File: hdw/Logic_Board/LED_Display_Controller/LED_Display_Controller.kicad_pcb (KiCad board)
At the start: 4 copper layers, 855 parts, among them J1101 USB_B_Mini, J1401 Encoder Ext, J1601 POS5P EXT, J1602 POS5P PGOOD, J1603 POS5P_THWN, J1604 POS5P_RUN, J201 +12V IN, J202 GND IN, J203 +12V IN AUX, J204 Master Power SW, J2901 STRING 1, J2902 STRING 2, J2903 STRING 3, J2904 STRING 4, J3001 USB UART, J3002 WIFI UART, J3003 FLASH SPI, J3004 Panel TP, J501 PICKIT3, J901 ESP8266 Socket, Q201 IPC100N04S51R7ATMA1, Q202 IPC100N04S51R7ATMA1, Q501 BSS214NW, Q901 BSS214NW, SW1401 Display Enable, SW1402 Brightness/Enable, SW501 MRST, U1001 ISO7321C, U1101 LT6700-1-S6, U1102 FT234XD, U1103 74LVC1G06, U1104 TPD3S014DBVR, U1201 74LVC1G06, U1202 74LVC1G06, U1203 74LVC1G06, U1204 74LVC1G06, U1205 74LVC1G06, U1206 74LVC1G06, U1207 74LVC1G06, U1301 74LVC1G06, U1302 74LVC1G06, U1303 74LVC1G06, U1304 74LVC1G06, U1401 MAX6816, U1402 74LVC2G14, U1403 74LVC1G79, U1601 LM1117-ADJ, U1602 NUP2202, U1603 74LVC1G17, U1604 74LVC1G17, U1605 74LVC1G17, U1606 NUP2202, U1701 CY7C1010DV33, U1801 SST25PF020B, U1901 SST25PF020B, U2001 SST25PF020B, U201 LTC4365DDB, U2101 SST25PF020B, U2201 SST25PF020B, U2301 SST25PF020B, U2401 SST25PF020B, U2501 SST25PF020B, U2601 74HCT541, U2602 74HCT541, U2701 74HCT541, U2702 74HCT541, U2801 74LVC1G32, U2802 74HCT541, U301 LTC3605A_UF, U401 LTC3624DD, U601 PIC32MZ2048EFH144_IPL

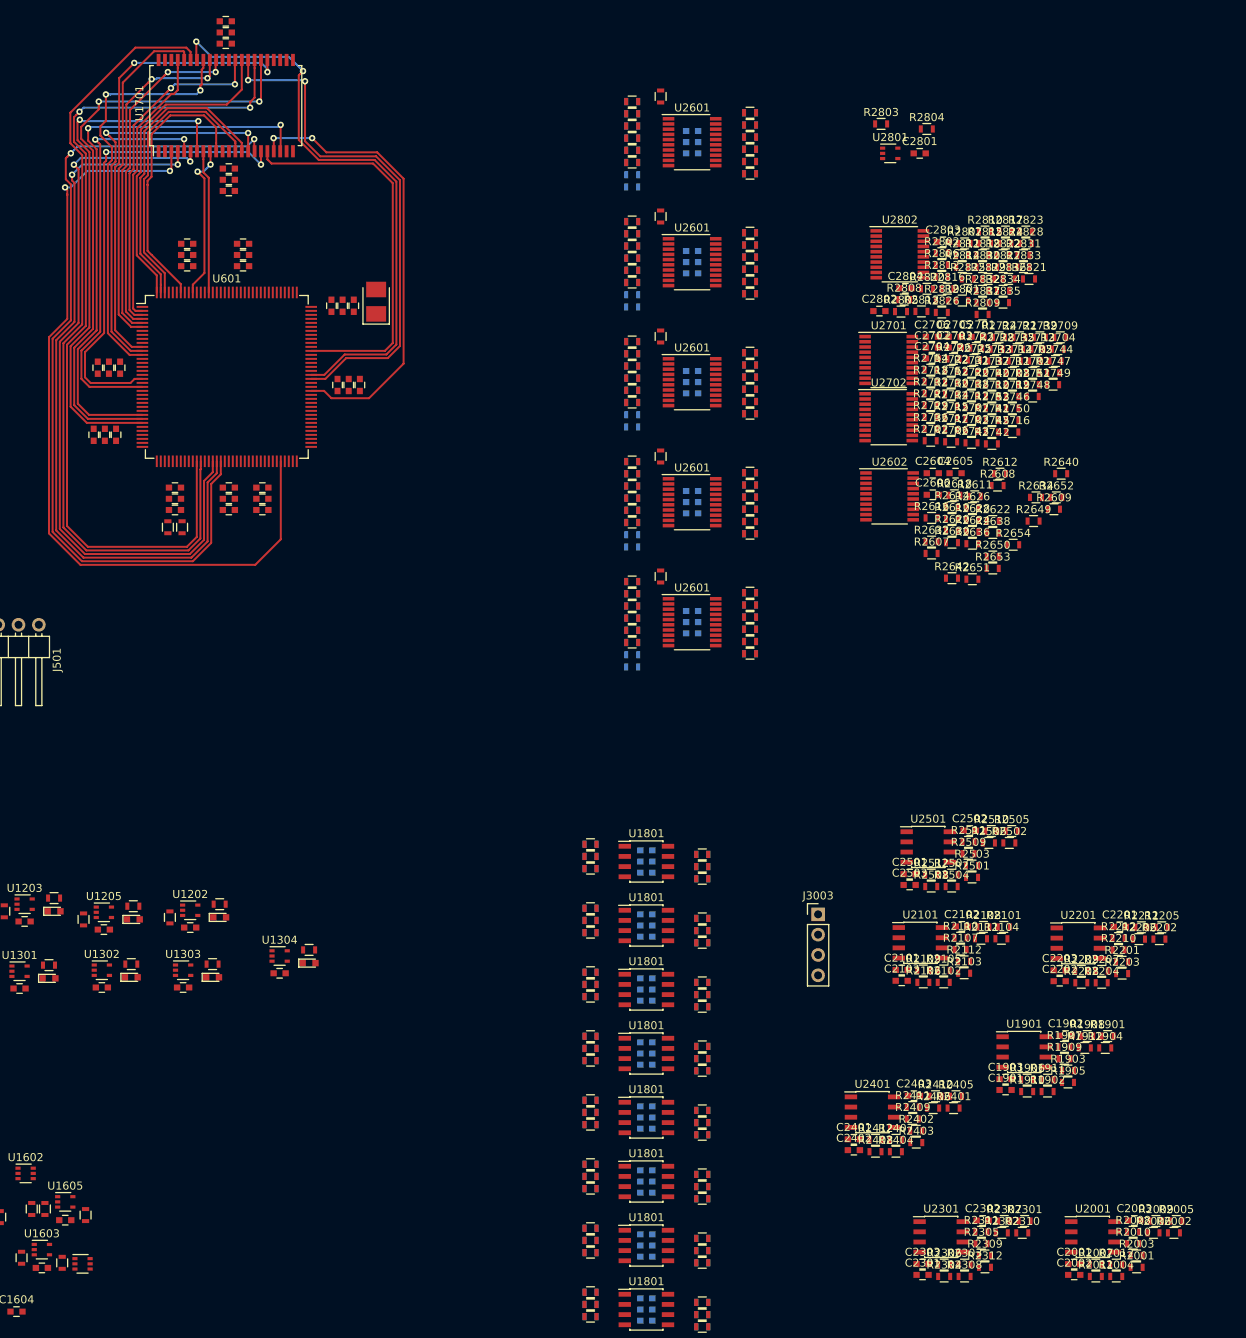
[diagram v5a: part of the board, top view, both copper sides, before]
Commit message: Fixed FLASH reference designators
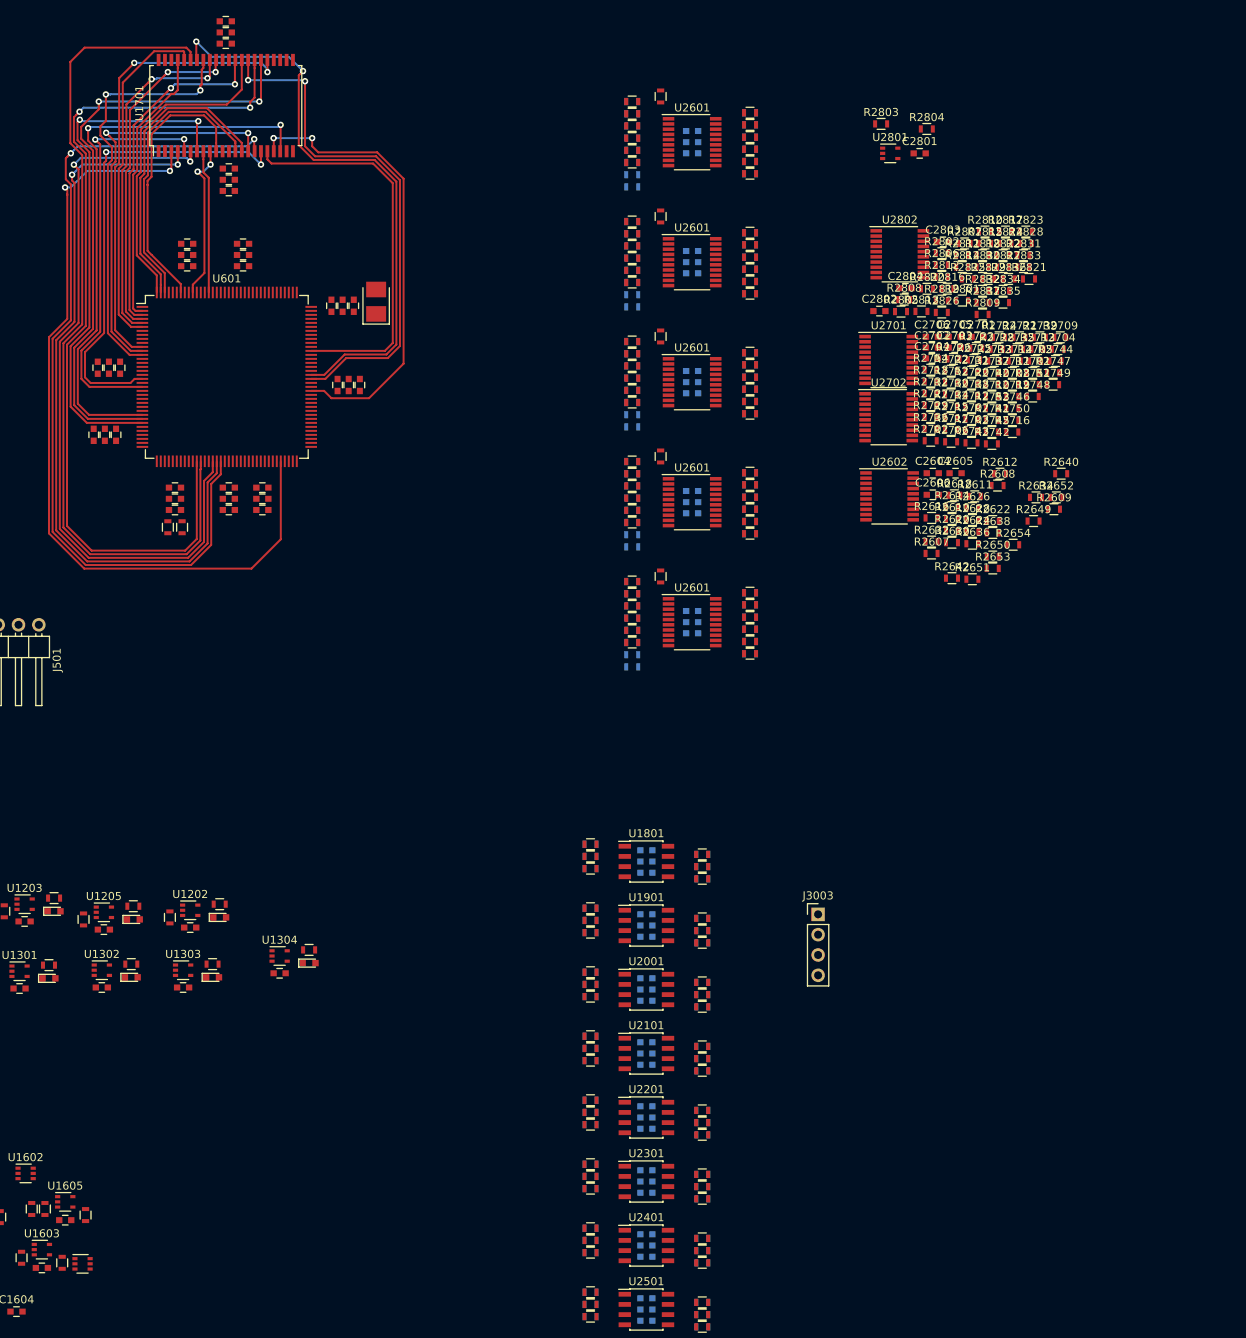
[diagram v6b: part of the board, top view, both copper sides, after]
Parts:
- removed the C1901 at (168.2, 156.6)
- removed the C1902 at (175.7, 149.8)
- removed the C1903 at (168.2, 155.2)
- removed the C2001 at (176.8, 178.3)
- removed the C2002 at (176.8, 179.7)
- removed the C2003 at (184.3, 172.9)
- removed the C2101 at (155.2, 141.6)
- removed the C2102 at (162.7, 136.1)
- removed the C2103 at (155.2, 142.9)
- removed the C2201 at (182.5, 136.2)
- removed the C2202 at (175.0, 143.0)
- removed the C2203 at (175.0, 141.6)
- removed the C2301 at (157.8, 179.7)
- removed the C2302 at (165.3, 172.9)
- removed the C2303 at (157.8, 178.3)
- removed the C2401 at (149.3, 162.7)
- removed the C2402 at (149.3, 164.1)
- removed the C2403 at (156.8, 157.3)
- removed the C2501 at (156.2, 129.6)
- removed the C2502 at (163.7, 124.1)
- removed the C2503 at (156.2, 130.9)
- removed the R1901 at (181.0, 149.8)
- removed the R1902 at (173.5, 156.8)
- removed the R1903 at (176.0, 154.1)
- removed the R1904 at (180.7, 151.3)
- removed the R1905 at (176.0, 155.6)
- removed the R1906 at (170.9, 155.3)
- removed the R1907 at (175.6, 151.2)
- removed the R1908 at (178.4, 149.8)
- removed the R1909 at (175.6, 152.7)
- removed the R1910 at (170.9, 156.8)
- removed the R1911 at (173.5, 155.3)
- removed the R1912 at (178.1, 151.3)
- removed the R2001 at (184.6, 178.7)
- removed the R2002 at (189.3, 174.4)
- removed the R2003 at (184.6, 177.3)
- removed the R2004 at (182.0, 179.9)
- removed the R2005 at (189.6, 173.0)
- removed the R2006 at (186.7, 174.4)
- removed the R2007 at (179.5, 178.4)
- removed the R2008 at (184.2, 174.3)
- removed the R2009 at (187.0, 173.0)
- removed the R2010 at (184.2, 175.8)
- removed the R2011 at (179.5, 179.9)
- removed the R2012 at (182.0, 178.4)
- removed the R2101 at (168.0, 136.2)
- removed the R2102 at (160.5, 143.1)
- removed the R2103 at (163.0, 142.0)
- removed the R2104 at (167.7, 137.7)
- removed the R2105 at (160.5, 141.6)
- removed the R2106 at (157.9, 143.1)
- removed the R2107 at (162.6, 139.0)
- removed the R2108 at (165.4, 136.2)
- removed the R2109 at (157.9, 141.6)
- removed the R2110 at (162.6, 137.5)
- removed the R2111 at (165.1, 137.7)
- removed the R2112 at (163.0, 140.5)
- removed the R2201 at (182.8, 140.5)
- removed the R2202 at (187.4, 137.7)
- removed the R2203 at (182.8, 142.0)
- removed the R2204 at (180.2, 143.2)
- removed the R2205 at (187.7, 136.2)
- removed the R2206 at (184.9, 137.7)
- removed the R2207 at (180.2, 141.7)
- removed the R2208 at (177.7, 143.2)
- removed the R2209 at (177.7, 141.7)
- removed the R2210 at (182.3, 139.1)
- removed the R2211 at (185.2, 136.2)
- removed the R2212 at (182.3, 137.6)
- removed the R2301 at (170.6, 173.0)
- removed the R2302 at (167.7, 174.4)
- removed the R2303 at (163.1, 178.4)
- removed the R2304 at (160.5, 179.9)
- removed the R2305 at (165.2, 175.8)
- removed the R2306 at (160.5, 178.4)
- removed the R2307 at (168.0, 173.0)
- removed the R2308 at (163.1, 179.9)
- removed the R2309 at (165.6, 177.3)
- removed the R2310 at (170.3, 174.4)
- removed the R2311 at (165.2, 174.3)
- removed the R2312 at (165.6, 178.7)
- removed the R2401 at (161.7, 158.8)
- removed the R2402 at (157.1, 161.7)
- removed the R2403 at (157.1, 163.1)
- removed the R2404 at (154.5, 164.3)
- removed the R2405 at (162.0, 157.4)
- removed the R2406 at (159.2, 158.8)
- removed the R2407 at (154.5, 162.8)
- removed the R2408 at (152.0, 164.3)
- removed the R2409 at (156.6, 160.2)
- removed the R2410 at (159.5, 157.4)
- removed the R2411 at (156.6, 158.7)
- removed the R2412 at (152.0, 162.8)
- removed the R2501 at (164.0, 130.0)
- removed the R2502 at (168.7, 125.7)
- removed the R2503 at (164.0, 128.5)
- removed the R2504 at (161.5, 131.1)
- removed the R2505 at (169.0, 124.2)
- removed the R2506 at (166.1, 125.7)
- removed the R2507 at (161.5, 129.7)
- removed the R2508 at (158.9, 131.1)
- removed the R2509 at (163.6, 127.0)
- removed the R2510 at (166.4, 124.2)
- removed the R2511 at (163.6, 125.6)
- removed the R2512 at (158.9, 129.7)
- removed the U1901 at (170.5, 151.8)
- removed the U2001 at (179.1, 174.9)
- removed the U2101 at (157.6, 138.2)
- removed the U2201 at (177.3, 138.2)
- removed the U2301 at (160.2, 174.9)
- removed the U2401 at (151.6, 159.3)
- removed the U2501 at (158.6, 126.2)
- renumbered C1801 to C1901, C1802 to C1902, C1803 to C1903, C1801 to C2001, C1802 to C2002, C1803 to C2003, C1801 to C2101, C1802 to C2102, C1803 to C2103, C1801 to C2201, C1802 to C2202, C1803 to C2203, C1801 to C2301, C1802 to C2302, C1803 to C2303, C1801 to C2401, C1802 to C2402, C1803 to C2403, C1801 to C2501, C1802 to C2502, C1803 to C2503, R1801 to R1901, R1802 to R1902, R1803 to R1903, R1804 to R1904, R1805 to R1905, R1806 to R1906, R1807 to R1907, R1808 to R1908, R1809 to R1909, R1810 to R1910, R1811 to R1911, R1812 to R1912, R1801 to R2001, R1802 to R2002, R1803 to R2003, R1804 to R2004, R1805 to R2005, R1806 to R2006, R1807 to R2007, R1808 to R2008, R1809 to R2009, R1810 to R2010, R1811 to R2011, R1812 to R2012, R1801 to R2101, R1802 to R2102, R1803 to R2103, R1804 to R2104, R1805 to R2105, R1806 to R2106, R1807 to R2107, R1808 to R2108, R1809 to R2109, R1810 to R2110, R1811 to R2111, R1812 to R2112, R1801 to R2201, R1802 to R2202, R1803 to R2203, R1804 to R2204, R1805 to R2205, R1806 to R2206, R1807 to R2207, R1808 to R2208, R1809 to R2209, R1810 to R2210, R1811 to R2211, R1812 to R2212, R1801 to R2301, R1802 to R2302, R1803 to R2303, R1804 to R2304, R1805 to R2305, R1806 to R2306, R1807 to R2307, R1808 to R2308, R1809 to R2309, R1810 to R2310, R1811 to R2311, R1812 to R2312, R1801 to R2401, R1802 to R2402, R1803 to R2403, R1804 to R2404, R1805 to R2405, R1806 to R2406, R1807 to R2407, R1808 to R2408, R1809 to R2409, R1810 to R2410, R1811 to R2411, R1812 to R2412, R1801 to R2501, R1802 to R2502, R1803 to R2503, R1804 to R2504, R1805 to R2505, R1806 to R2506, R1807 to R2507, R1808 to R2508, R1809 to R2509, R1810 to R2510, R1811 to R2511, R1812 to R2512, U1801 to U1901, U1801 to U2001, U1801 to U2101, U1801 to U2201, U1801 to U2301, U1801 to U2401, U1801 to U2501
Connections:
- R1901 pad 1: Net-(R1801-Pad1) -> Net-(R1901-Pad1)
- R1902 pad 1: Net-(R1802-Pad1) -> Net-(R1902-Pad1)
- R1903 pad 1: Net-(R1803-Pad1) -> Net-(R1903-Pad1)
- R1903 pad 2: ~FLASH_WP1 -> ~FLASH_WP2
- R1904 pad 1: Net-(R1804-Pad1) -> Net-(R1904-Pad1)
- R1904 pad 2: ~FLASH_CE1 -> ~FLASH_CE2
- R1905 pad 1: Net-(R1805-Pad1) -> Net-(R1905-Pad1)
- R1906 pad 2: Net-(R1803-Pad1) -> Net-(R1903-Pad1)
- R1907 pad 2: Net-(R1804-Pad1) -> Net-(R1904-Pad1)
- R1908 pad 1: Net-(R1805-Pad1) -> Net-(R1905-Pad1)
- R1909 pad 2: Net-(R1802-Pad1) -> Net-(R1902-Pad1)
- R1910 pad 1: Net-(R1801-Pad1) -> Net-(R1901-Pad1)
- R1911 pad 1: Net-(R1811-Pad1) -> Net-(R1911-Pad1)
- R1912 pad 2: Net-(R1811-Pad1) -> Net-(R1911-Pad1)
- R2001 pad 1: Net-(R1801-Pad1) -> Net-(R2001-Pad1)
- R2002 pad 1: Net-(R1802-Pad1) -> Net-(R2002-Pad1)
- R2003 pad 1: Net-(R1803-Pad1) -> Net-(R2003-Pad1)
- R2003 pad 2: ~FLASH_WP1 -> ~FLASH_WP3
- R2004 pad 1: Net-(R1804-Pad1) -> Net-(R2004-Pad1)
- R2004 pad 2: ~FLASH_CE1 -> ~FLASH_CE3
- R2005 pad 1: Net-(R1805-Pad1) -> Net-(R2005-Pad1)
- R2006 pad 2: Net-(R1803-Pad1) -> Net-(R2003-Pad1)
- R2007 pad 2: Net-(R1804-Pad1) -> Net-(R2004-Pad1)
- R2008 pad 1: Net-(R1805-Pad1) -> Net-(R2005-Pad1)
- R2009 pad 2: Net-(R1802-Pad1) -> Net-(R2002-Pad1)
- R2010 pad 1: Net-(R1801-Pad1) -> Net-(R2001-Pad1)
- R2011 pad 1: Net-(R1811-Pad1) -> Net-(R2011-Pad1)
- R2012 pad 2: Net-(R1811-Pad1) -> Net-(R2011-Pad1)
- R2101 pad 1: Net-(R1801-Pad1) -> Net-(R2101-Pad1)
- R2102 pad 1: Net-(R1802-Pad1) -> Net-(R2102-Pad1)
- R2103 pad 1: Net-(R1803-Pad1) -> Net-(R2103-Pad1)
- R2103 pad 2: ~FLASH_WP1 -> ~FLASH_WP4
- R2104 pad 1: Net-(R1804-Pad1) -> Net-(R2104-Pad1)
- R2104 pad 2: ~FLASH_CE1 -> ~FLASH_CE4
- R2105 pad 1: Net-(R1805-Pad1) -> Net-(R2105-Pad1)
- R2106 pad 2: Net-(R1803-Pad1) -> Net-(R2103-Pad1)
- R2107 pad 2: Net-(R1804-Pad1) -> Net-(R2104-Pad1)
- R2108 pad 1: Net-(R1805-Pad1) -> Net-(R2105-Pad1)
- R2109 pad 2: Net-(R1802-Pad1) -> Net-(R2102-Pad1)
- R2110 pad 1: Net-(R1801-Pad1) -> Net-(R2101-Pad1)
- R2111 pad 1: Net-(R1811-Pad1) -> Net-(R2111-Pad1)
- R2112 pad 2: Net-(R1811-Pad1) -> Net-(R2111-Pad1)
- R2201 pad 1: Net-(R1801-Pad1) -> Net-(R2201-Pad1)
- R2202 pad 1: Net-(R1802-Pad1) -> Net-(R2202-Pad1)
- R2203 pad 1: Net-(R1803-Pad1) -> Net-(R2203-Pad1)
- R2203 pad 2: ~FLASH_WP1 -> ~FLASH_WP5
- R2204 pad 1: Net-(R1804-Pad1) -> Net-(R2204-Pad1)
- R2204 pad 2: ~FLASH_CE1 -> ~FLASH_CE5
- R2205 pad 1: Net-(R1805-Pad1) -> Net-(R2205-Pad1)
- R2206 pad 2: Net-(R1803-Pad1) -> Net-(R2203-Pad1)
- R2207 pad 2: Net-(R1804-Pad1) -> Net-(R2204-Pad1)
- R2208 pad 1: Net-(R1805-Pad1) -> Net-(R2205-Pad1)
- R2209 pad 2: Net-(R1802-Pad1) -> Net-(R2202-Pad1)
- R2210 pad 1: Net-(R1801-Pad1) -> Net-(R2201-Pad1)
- R2211 pad 1: Net-(R1811-Pad1) -> Net-(R2211-Pad1)
- R2212 pad 2: Net-(R1811-Pad1) -> Net-(R2211-Pad1)
- R2301 pad 1: Net-(R1801-Pad1) -> Net-(R2301-Pad1)
- R2302 pad 1: Net-(R1802-Pad1) -> Net-(R2302-Pad1)
- R2303 pad 1: Net-(R1803-Pad1) -> Net-(R2303-Pad1)
- R2303 pad 2: ~FLASH_WP1 -> ~FLASH_WP6
- R2304 pad 1: Net-(R1804-Pad1) -> Net-(R2304-Pad1)
- R2304 pad 2: ~FLASH_CE1 -> ~FLASH_CE6
- R2305 pad 1: Net-(R1805-Pad1) -> Net-(R2305-Pad1)
- R2306 pad 2: Net-(R1803-Pad1) -> Net-(R2303-Pad1)
- R2307 pad 2: Net-(R1804-Pad1) -> Net-(R2304-Pad1)
- R2308 pad 1: Net-(R1805-Pad1) -> Net-(R2305-Pad1)
- R2309 pad 2: Net-(R1802-Pad1) -> Net-(R2302-Pad1)
- R2310 pad 1: Net-(R1801-Pad1) -> Net-(R2301-Pad1)
- R2311 pad 1: Net-(R1811-Pad1) -> Net-(R2311-Pad1)
- R2312 pad 2: Net-(R1811-Pad1) -> Net-(R2311-Pad1)
- R2401 pad 1: Net-(R1801-Pad1) -> Net-(R2401-Pad1)
- R2402 pad 1: Net-(R1802-Pad1) -> Net-(R2402-Pad1)
- R2403 pad 1: Net-(R1803-Pad1) -> Net-(R2403-Pad1)
- R2403 pad 2: ~FLASH_WP1 -> ~FLASH_WP7
- R2404 pad 1: Net-(R1804-Pad1) -> Net-(R2404-Pad1)
- R2404 pad 2: ~FLASH_CE1 -> ~FLASH_CE7
- R2405 pad 1: Net-(R1805-Pad1) -> Net-(R2405-Pad1)
- R2406 pad 2: Net-(R1803-Pad1) -> Net-(R2403-Pad1)
- R2407 pad 2: Net-(R1804-Pad1) -> Net-(R2404-Pad1)
- R2408 pad 1: Net-(R1805-Pad1) -> Net-(R2405-Pad1)
- R2409 pad 2: Net-(R1802-Pad1) -> Net-(R2402-Pad1)
- R2410 pad 1: Net-(R1801-Pad1) -> Net-(R2401-Pad1)
- R2411 pad 1: Net-(R1811-Pad1) -> Net-(R2411-Pad1)
- R2412 pad 2: Net-(R1811-Pad1) -> Net-(R2411-Pad1)
- R2501 pad 1: Net-(R1801-Pad1) -> Net-(R2501-Pad1)
- R2502 pad 1: Net-(R1802-Pad1) -> Net-(R2502-Pad1)
- R2503 pad 1: Net-(R1803-Pad1) -> Net-(R2503-Pad1)
- R2503 pad 2: ~FLASH_WP1 -> ~FLASH_WP8
- R2504 pad 1: Net-(R1804-Pad1) -> Net-(R2504-Pad1)
- R2504 pad 2: ~FLASH_CE1 -> ~FLASH_CE8
- R2505 pad 1: Net-(R1805-Pad1) -> Net-(R2505-Pad1)
- R2506 pad 2: Net-(R1803-Pad1) -> Net-(R2503-Pad1)
- R2507 pad 2: Net-(R1804-Pad1) -> Net-(R2504-Pad1)
- R2508 pad 1: Net-(R1805-Pad1) -> Net-(R2505-Pad1)
- R2509 pad 2: Net-(R1802-Pad1) -> Net-(R2502-Pad1)
- R2510 pad 1: Net-(R1801-Pad1) -> Net-(R2501-Pad1)
- R2511 pad 1: Net-(R1811-Pad1) -> Net-(R2511-Pad1)
- R2512 pad 2: Net-(R1811-Pad1) -> Net-(R2511-Pad1)
- U1901 pad 1: Net-(R1804-Pad1) -> Net-(R1904-Pad1)
- U1901 pad 2: Net-(R1811-Pad1) -> Net-(R1911-Pad1)
- U1901 pad 3: Net-(R1803-Pad1) -> Net-(R1903-Pad1)
- U1901 pad 5: Net-(R1801-Pad1) -> Net-(R1901-Pad1)
- U1901 pad 6: Net-(R1805-Pad1) -> Net-(R1905-Pad1)
- U1901 pad 7: Net-(R1802-Pad1) -> Net-(R1902-Pad1)
- U2001 pad 1: Net-(R1804-Pad1) -> Net-(R2004-Pad1)
- U2001 pad 2: Net-(R1811-Pad1) -> Net-(R2011-Pad1)
- U2001 pad 3: Net-(R1803-Pad1) -> Net-(R2003-Pad1)
- U2001 pad 5: Net-(R1801-Pad1) -> Net-(R2001-Pad1)
- U2001 pad 6: Net-(R1805-Pad1) -> Net-(R2005-Pad1)
- U2001 pad 7: Net-(R1802-Pad1) -> Net-(R2002-Pad1)
- U2101 pad 1: Net-(R1804-Pad1) -> Net-(R2104-Pad1)
- U2101 pad 2: Net-(R1811-Pad1) -> Net-(R2111-Pad1)
- U2101 pad 3: Net-(R1803-Pad1) -> Net-(R2103-Pad1)
- U2101 pad 5: Net-(R1801-Pad1) -> Net-(R2101-Pad1)
- U2101 pad 6: Net-(R1805-Pad1) -> Net-(R2105-Pad1)
- U2101 pad 7: Net-(R1802-Pad1) -> Net-(R2102-Pad1)
- U2201 pad 1: Net-(R1804-Pad1) -> Net-(R2204-Pad1)
- U2201 pad 2: Net-(R1811-Pad1) -> Net-(R2211-Pad1)
- U2201 pad 3: Net-(R1803-Pad1) -> Net-(R2203-Pad1)
- U2201 pad 5: Net-(R1801-Pad1) -> Net-(R2201-Pad1)
- U2201 pad 6: Net-(R1805-Pad1) -> Net-(R2205-Pad1)
- U2201 pad 7: Net-(R1802-Pad1) -> Net-(R2202-Pad1)
- U2301 pad 1: Net-(R1804-Pad1) -> Net-(R2304-Pad1)
- U2301 pad 2: Net-(R1811-Pad1) -> Net-(R2311-Pad1)
- U2301 pad 3: Net-(R1803-Pad1) -> Net-(R2303-Pad1)
- U2301 pad 5: Net-(R1801-Pad1) -> Net-(R2301-Pad1)
- U2301 pad 6: Net-(R1805-Pad1) -> Net-(R2305-Pad1)
- U2301 pad 7: Net-(R1802-Pad1) -> Net-(R2302-Pad1)
- U2401 pad 1: Net-(R1804-Pad1) -> Net-(R2404-Pad1)
- U2401 pad 2: Net-(R1811-Pad1) -> Net-(R2411-Pad1)
- U2401 pad 3: Net-(R1803-Pad1) -> Net-(R2403-Pad1)
- U2401 pad 5: Net-(R1801-Pad1) -> Net-(R2401-Pad1)
- U2401 pad 6: Net-(R1805-Pad1) -> Net-(R2405-Pad1)
- U2401 pad 7: Net-(R1802-Pad1) -> Net-(R2402-Pad1)
- U2501 pad 1: Net-(R1804-Pad1) -> Net-(R2504-Pad1)
- U2501 pad 2: Net-(R1811-Pad1) -> Net-(R2511-Pad1)
- U2501 pad 3: Net-(R1803-Pad1) -> Net-(R2503-Pad1)
- U2501 pad 5: Net-(R1801-Pad1) -> Net-(R2501-Pad1)
- U2501 pad 6: Net-(R1805-Pad1) -> Net-(R2505-Pad1)
- U2501 pad 7: Net-(R1802-Pad1) -> Net-(R2502-Pad1)
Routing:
- net EBI_A7: track 101.7 -> 105.9 mm
- net EBI_A14: track 56.8 -> 57.4 mm
- net EBI_A10: track 108.7 -> 109.2 mm
- net EBI_A1: track 93.5 -> 94.0 mm
- net EBI_A3: track 92.6 -> 93.1 mm
- net EBI_A17: track 107.0 -> 107.5 mm
